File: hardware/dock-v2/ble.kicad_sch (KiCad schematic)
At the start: 11 parts, among them U501 ESP32-C3-MINI-1-H4X

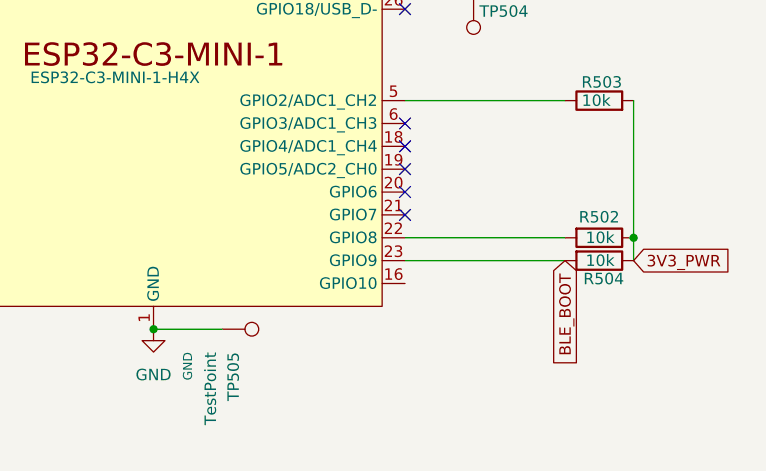
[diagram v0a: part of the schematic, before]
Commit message: Dock v2 schematic: pogo sheet wired, fixes from review (user's work, snapshot)
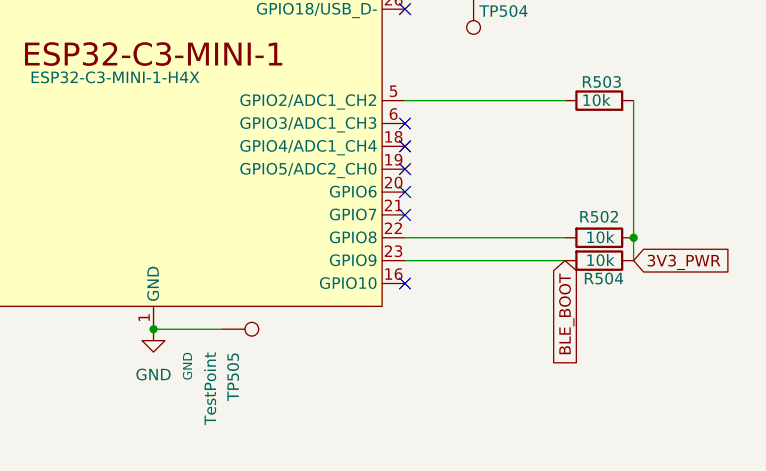
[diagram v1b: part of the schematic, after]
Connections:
- no-connect marks 9 -> 10
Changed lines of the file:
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@@
+	)
+	(no_connect
+		(at 148.59 124.46)
 	)
 	(no_connect
